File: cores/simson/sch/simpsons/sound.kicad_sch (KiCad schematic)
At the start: 18 parts

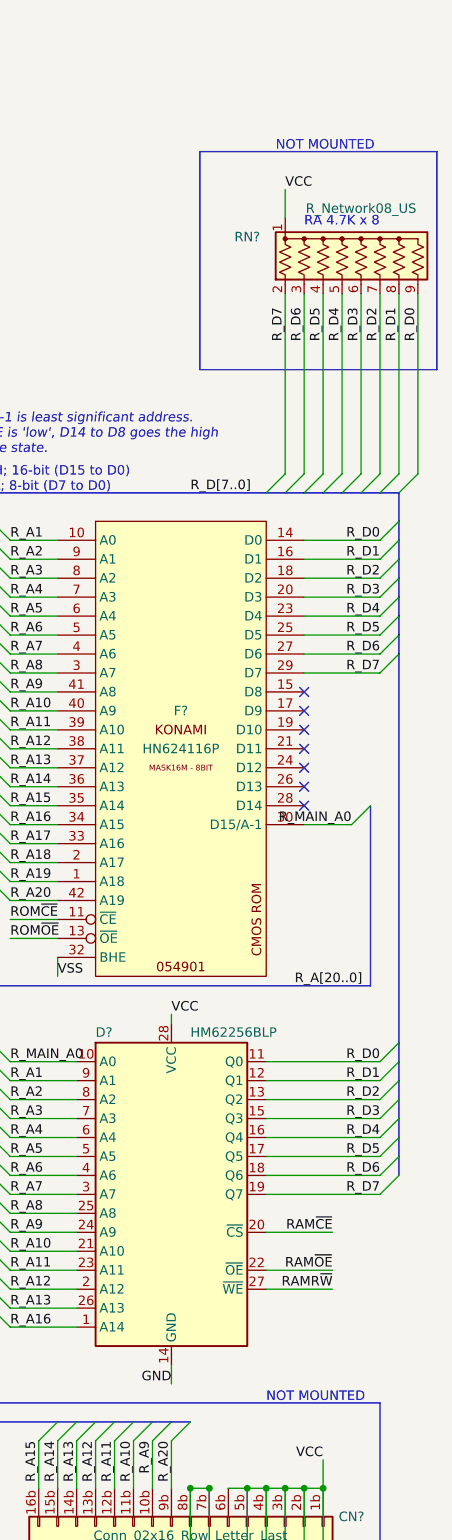
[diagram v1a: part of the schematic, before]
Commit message: sch: not mounted -> not populated
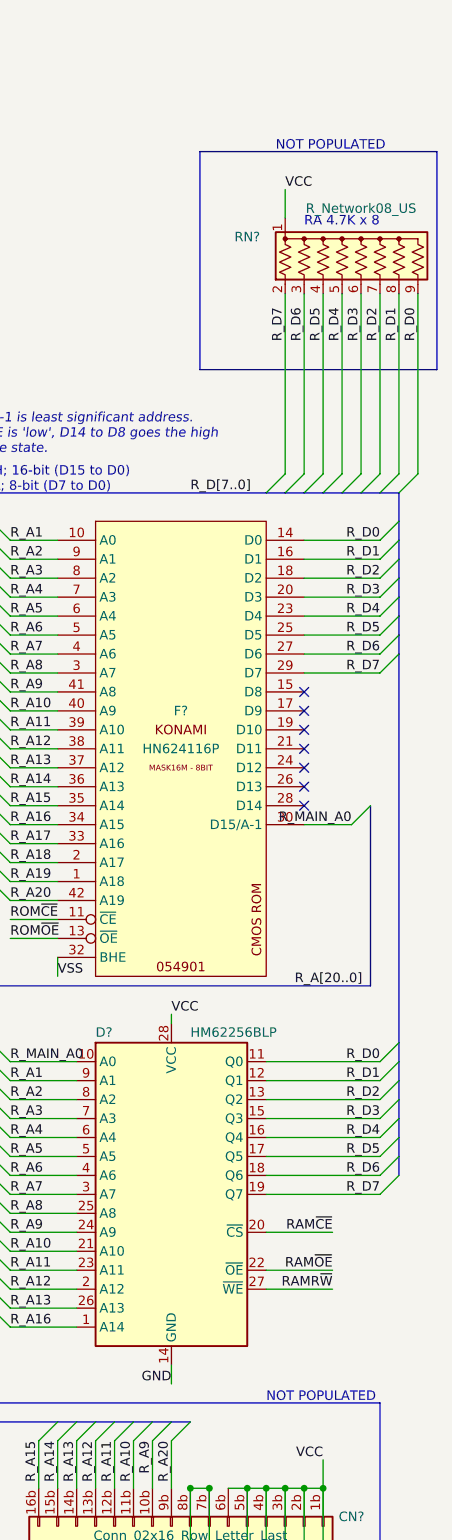
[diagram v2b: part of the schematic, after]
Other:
- note added: "NOT POPULATED"
- note removed: "NOT MOUNTED"
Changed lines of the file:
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@@
     (effects (font (size 1.27 1.27) (thickness 0.254) bold) (justify left bottom))
   )
-  (text "NOT MOUNTED\n" (at 381 212.09 0)
+  (text "NOT POPULATED\n" (at 381 212.09 0)
     (effects (font (size 1.27 1.27)) (justify left bottom))
   )
@@
     (effects (font (size 1.27 1.27) (thickness 0.254) bold) (justify left bottom))
   )
-  (text "NOT MOUNTED\n" (at 382.27 44.45 0)
+  (text "NOT POPULATED\n" (at 382.27 44.45 0)
     (effects (font (size 1.27 1.27)) (justify left bottom))
   )
